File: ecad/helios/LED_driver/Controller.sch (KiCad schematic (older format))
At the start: 12 parts, among them J3 Conn_02x03_Odd_Even, SW1 SW_Push, U7 ATTINY24-20SSU, Y1 Crystal

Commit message: Finishes the schematics
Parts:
- J4: renamed from J3; Part Number (none) -> M20-8760342
- SW1: footprint (none) -> Buttons_Switches_THT:SW_PUSH_6mm; Part Number (none) -> 1825910-6
- Y1: value Crystal -> 10 MHz; Part Number (none) -> ABLS-10.000MHZ-B2-T
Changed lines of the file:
@@
 P 7000 4650
 F 0 "Y1" H 7000 4800 50  0000 C CNN
-F 1 "Crystal" H 7000 4500 50  0000 C CNN
+F 1 "10 MHz" H 7000 4500 50  0000 C CNN
 F 2 "Crystals:Crystal_SMD_HC49-SD" H 7000 4650 50  0001 C CNN
 F 3 "" H 7000 4650 50  0001 C CNN
+F 4 "ABLS-10.000MHZ-B2-T" H 7000 4650 60  0001 C CNN "Part Number"
 	1    7000 4650
 	0    1    1    0
@@
 	7700 4950 7500 4950
 $Comp
-L GND #PWR026
+L GND #PWR027
 U 1 1 5AB48C0D
 P 7900 4650
-F 0 "#PWR026" H 7900 4400 50  0001 C CNN
+F 0 "#PWR027" H 7900 4400 50  0001 C CNN
 F 1 "GND" H 7900 4500 50  0000 C CNN
 F 2 "" H 7900 4650 50  0001 C CNN
@@
 Connection ~ 7000 4850
 $Comp
-L Conn_02x03_Odd_Even J3
+L Conn_02x03_Odd_Even J4
 U 1 1 5AB48E51
 P 7300 2400
-F 0 "J3" H 7350 2600 50  0000 C CNN
+F 0 "J4" H 7350 2600 50  0000 C CNN
 F 1 "Conn_02x03_Odd_Even" H 7350 2200 50  0000 C CNN
 F 2 "Pin_Headers:Pin_Header_Straight_2x03_Pitch2.54mm_SMD" H 7300 2400 50  0001 C CNN
 F 3 "" H 7300 2400 50  0001 C CNN
+F 4 "M20-8760342" H 7300 2400 60  0001 C CNN "Part Number"
 	1    7300 2400
 	1    0    0    -1
@@
 	6500 2500 7100 2500
 $Comp
-L +5V #PWR027
+L +5V #PWR028
 U 1 1 5AB48FA1
 P 8050 2000
-F 0 "#PWR027" H 8050 1850 50  0001 C CNN
+F 0 "#PWR028" H 8050 1850 50  0001 C CNN
 F 1 "+5V" H 8050 2140 50  0000 C CNN
 F 2 "" H 8050 2000 50  0001 C CNN
@@
 	8050 2300 7600 2300
 $Comp
-L GND #PWR028
+L GND #PWR029
 U 1 1 5AB48FDE
 P 8050 2900
-F 0 "#PWR028" H 8050 2650 50  0001 C CNN
+F 0 "#PWR029" H 8050 2650 50  0001 C CNN
 F 1 "GND" H 8050 2750 50  0000 C CNN
 F 2 "" H 8050 2900 50  0001 C CNN
@@
 	2300 4900 2600 4900
 $Comp
-L +36V #PWR029
+L +36V #PWR030
 U 1 1 5AB49787
 P 6000 2350
-F 0 "#PWR029" H 6000 2200 50  0001 C CNN
+F 0 "#PWR030" H 6000 2200 50  0001 C CNN
 F 1 "+36V" H 6000 2490 50  0000 C CNN
 F 2 "" H 6000 2350 50  0001 C CNN
@@
 $EndComp
 $Comp
-L GND #PWR030
+L GND #PWR031
 U 1 1 5AB49BA2
 P 6000 3450
-F 0 "#PWR030" H 6000 3200 50  0001 C CNN
+F 0 "#PWR031" H 6000 3200 50  0001 C CNN
 F 1 "GND" H 6000 3300 50  0000 C CNN
 F 2 "" H 6000 3450 50  0001 C CNN
@@
 Connection ~ 2300 3700
 $Comp
-L +5V #PWR031
+L +5V #PWR032
 U 1 1 5AB49D08
 P 2300 2800
-F 0 "#PWR031" H 2300 2650 50  0001 C CNN
+F 0 "#PWR032" H 2300 2650 50  0001 C CNN
 F 1 "+5V" H 2300 2940 50  0000 C CNN
 F 2 "" H 2300 2800 50  0001 C CNN
@@
 F 0 "SW1" H 4500 5950 50  0000 L CNN
 F 1 "SW_Push" H 4450 5790 50  0000 C CNN
-F 2 "" H 4450 6050 50  0001 C CNN
+F 2 "Buttons_Switches_THT:SW_PUSH_6mm" H 4450 6050 50  0001 C CNN
 F 3 "" H 4450 6050 50  0001 C CNN
+F 4 "1825910-6" H 4450 5850 60  0001 C CNN "Part Number"
 	1    4450 5850
 	1    0    0    -1
@@
 	5200 5200 5200 5400
 $Comp
-L +5V #PWR032
+L +5V #PWR033
 U 1 1 5AB4A50E
 P 5050 5150
-F 0 "#PWR032" H 5050 5000 50  0001 C CNN
+F 0 "#PWR033" H 5050 5000 50  0001 C CNN
 F 1 "+5V" H 5050 5290 50  0000 C CNN
 F 2 "" H 5050 5150 50  0001 C CNN
@@
 Connection ~ 4900 5850
 $Comp
-L GND #PWR033
+L GND #PWR034
 U 1 1 5AB4A605
 P 4000 6050
-F 0 "#PWR033" H 4000 5800 50  0001 C CNN
+F 0 "#PWR034" H 4000 5800 50  0001 C CNN
 F 1 "GND" H 4000 5900 50  0000 C CNN
 F 2 "" H 4000 6050 50  0001 C CNN

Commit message: layouted the board
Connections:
- net EN36V: now also U7.11 ((PCINT2/AIN1/ADC2)PA2); no longer U7.12 ((PCINT1/AIN0/ADC1)PA1)
- net FLASH_IN: now also U7.13 ((PCINT0/AREF/ADC0)PA0); no longer U7.10 ((PCINT3/T0/ADC3)PA3)
- net GND: now also C36.2, U7.14 (GND)
- net IR_ON: now also U7.10 ((PCINT3/T0/ADC3)PA3); no longer U7.11 ((PCINT2/AIN1/ADC2)PA2)
- net V36_MEASURE: now reaches D8.2 (A), R36.2, R37.1
- net V36_MEASURE: now also U7.12 ((PCINT1/AIN0/ADC1)PA1); no longer U7.13 ((PCINT0/AREF/ADC0)PA0)
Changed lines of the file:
@@
 	4700 4100 5100 4100
 Wire Wire Line
-	4700 4200 5100 4200
+	4700 4200 5650 4200
 Wire Wire Line
 	4700 4900 6100 4900
@@
 Wire Wire Line
 	2300 3700 2600 3700
-Wire Wire Line
-	2300 4400 2300 4900
-Wire Wire Line
-	2300 4900 2600 4900
 $Comp
 L +36V #PWR030
@@
 Wire Wire Line
 	6000 2900 5750 2900
-Wire Wire Line
-	5750 2900 5750 3700
-Wire Wire Line
-	5750 3700 4700 3700
 Connection ~ 6000 2900
 Wire Wire Line
-	4400 3150 4950 3150
-Wire Wire Line
-	4950 3150 4950 3700
-Connection ~ 4950 3700
+	4400 3150 5750 3150
 Wire Wire Line
 	4100 3150 2300 3150
@@
 Text HLabel 5650 4300 2    60   Input ~ 0
 DATA_IN
-Text HLabel 5650 4000 2    60   Input ~ 0
+Text HLabel 5050 3700 2    60   Input ~ 0
 FLASH_IN
 Text HLabel 5650 4800 2    60   Output ~ 0
@@
 	4700 4800 5650 4800
 Wire Wire Line
-	4700 4000 5650 4000
-Wire Wire Line
 	4700 4300 5650 4300
-Text HLabel 5650 3900 2    60   Output ~ 0
+Text HLabel 5050 4000 2    60   Output ~ 0
 IR_ON
-Wire Wire Line
-	4700 3900 5650 3900
 NoConn ~ 4700 4400
-Text HLabel 5650 3800 2    60   Output ~ 0
+Text HLabel 5050 3900 2    60   Output ~ 0
 EN36V
-Wire Wire Line
-	4700 3800 5650 3800
+Connection ~ 5750 3150
+Text Label 4800 3150 0    60   ~ 0
+V36_MEASURE
+Wire Wire Line
+	4700 4000 5050 4000
+Wire Wire Line
+	4700 3800 5750 3800
+$Comp
+L GND #PWR035
+U 1 1 5AB6BFF7
+P 2300 5050
+F 0 "#PWR035" H 2300 4800 50  0001 C CNN
+F 1 "GND" H 2300 4900 50  0000 C CNN
+F 2 "" H 2300 5050 50  0001 C CNN
+F 3 "" H 2300 5050 50  0001 C CNN
+	1    2300 5050
+	1    0    0    -1
+$EndComp
+Wire Wire Line
+	2300 4400 2300 5050
+Wire Wire Line
+	2600 4900 2300 4900
+Connection ~ 2300 4900
+Wire Wire Line
+	4700 3700 5050 3700
+Wire Wire Line
+	5750 3800 5750 2900
+Wire Wire Line
+	4700 3900 5050 3900
 $EndSCHEMATC

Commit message: Improves the layout
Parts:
- added R12: 100, Resistors_SMD:R_0603, symbol R
- Y1: footprint Crystals:Crystal_SMD_HC49-SD -> Crystals:Crystal_SMD_TXC_7M-4pin_3.2x2.5mm; Part Number ABLS-10.000MHZ-B2-T -> 7V-10.000MAHJ-T
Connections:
- net DATA_IN: now also R12.1; no longer J4.4 (Pin_4), U7.7 ((PCINT6/SDA/DI/MOSI/OC1A/ADC6)PA6)
- net EN36V: now also U7.10 ((PCINT3/T0/ADC3)PA3); no longer U7.11 ((PCINT2/AIN1/ADC2)PA2)
- net FLASH_IN: now also U7.6 ((PCINT7/ICP/OC0B/ADC7)PA7); no longer U7.13 ((PCINT0/AREF/ADC0)PA0)
- net IR_ON: now also U7.11 ((PCINT2/AIN1/ADC2)PA2); no longer U7.10 ((PCINT3/T0/ADC3)PA3)
- new net ICSP_MOSI: J4.4 (Pin_4), R12.2, U7.7 ((PCINT6/SDA/DI/MOSI/OC1A/ADC6)PA6)
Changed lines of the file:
@@
 F 0 "Y1" H 7000 4800 50  0000 C CNN
 F 1 "10 MHz" H 7000 4500 50  0000 C CNN
-F 2 "Crystals:Crystal_SMD_HC49-SD" H 7000 4650 50  0001 C CNN
+F 2 "Crystals:Crystal_SMD_TXC_7M-4pin_3.2x2.5mm" H 7000 4650 50  0001 C CNN
 F 3 "" H 7000 4650 50  0001 C CNN
-F 4 "ABLS-10.000MHZ-B2-T" H 7000 4650 60  0001 C CNN "Part Number"
+F 4 "7V-10.000MAHJ-T" H 7000 4650 60  0001 C CNN "Part Number"
 	1    7000 4650
 	0    1    1    0
@@
 	7700 4950 7500 4950
 $Comp
-L GND #PWR027
+L GND #PWR031
 U 1 1 5AB48C0D
 P 7900 4650
-F 0 "#PWR027" H 7900 4400 50  0001 C CNN
+F 0 "#PWR031" H 7900 4400 50  0001 C CNN
 F 1 "GND" H 7900 4500 50  0000 C CNN
 F 2 "" H 7900 4650 50  0001 C CNN
@@
 	6500 2500 7100 2500
 $Comp
-L +5V #PWR028
+L +5V #PWR032
 U 1 1 5AB48FA1
 P 8050 2000
-F 0 "#PWR028" H 8050 1850 50  0001 C CNN
+F 0 "#PWR032" H 8050 1850 50  0001 C CNN
 F 1 "+5V" H 8050 2140 50  0000 C CNN
 F 2 "" H 8050 2000 50  0001 C CNN
@@
 	8050 2300 7600 2300
 $Comp
-L GND #PWR029
+L GND #PWR033
 U 1 1 5AB48FDE
 P 8050 2900
-F 0 "#PWR029" H 8050 2650 50  0001 C CNN
+F 0 "#PWR033" H 8050 2650 50  0001 C CNN
 F 1 "GND" H 8050 2750 50  0000 C CNN
 F 2 "" H 8050 2900 50  0001 C CNN
@@
 	2300 3700 2600 3700
 $Comp
-L +36V #PWR030
+L +36V #PWR034
 U 1 1 5AB49787
 P 6000 2350
-F 0 "#PWR030" H 6000 2200 50  0001 C CNN
+F 0 "#PWR034" H 6000 2200 50  0001 C CNN
 F 1 "+36V" H 6000 2490 50  0000 C CNN
 F 2 "" H 6000 2350 50  0001 C CNN
@@
 $EndComp
 $Comp
-L GND #PWR031
+L GND #PWR035
 U 1 1 5AB49BA2
 P 6000 3450
-F 0 "#PWR031" H 6000 3200 50  0001 C CNN
+F 0 "#PWR035" H 6000 3200 50  0001 C CNN
 F 1 "GND" H 6000 3300 50  0000 C CNN
 F 2 "" H 6000 3450 50  0001 C CNN
@@
 Connection ~ 2300 3700
 $Comp
-L +5V #PWR032
+L +5V #PWR036
 U 1 1 5AB49D08
 P 2300 2800
-F 0 "#PWR032" H 2300 2650 50  0001 C CNN
+F 0 "#PWR036" H 2300 2650 50  0001 C CNN
 F 1 "+5V" H 2300 2940 50  0000 C CNN
 F 2 "" H 2300 2800 50  0001 C CNN
@@
 	5200 5200 5200 5400
 $Comp
-L +5V #PWR033
+L +5V #PWR037
 U 1 1 5AB4A50E
 P 5050 5150
-F 0 "#PWR033" H 5050 5000 50  0001 C CNN
+F 0 "#PWR037" H 5050 5000 50  0001 C CNN
 F 1 "+5V" H 5050 5290 50  0000 C CNN
 F 2 "" H 5050 5150 50  0001 C CNN
@@
 Connection ~ 4900 5850
 $Comp
-L GND #PWR034
+L GND #PWR038
 U 1 1 5AB4A605
 P 4000 6050
-F 0 "#PWR034" H 4000 5800 50  0001 C CNN
+F 0 "#PWR038" H 4000 5800 50  0001 C CNN
 F 1 "GND" H 4000 5900 50  0000 C CNN
 F 2 "" H 4000 6050 50  0001 C CNN
@@
 Wire Wire Line
 	4000 5850 4250 5850
-Text HLabel 5650 4300 2    60   Input ~ 0
+Text HLabel 6450 4300 2    60   Input ~ 0
 DATA_IN
-Text HLabel 5050 3700 2    60   Input ~ 0
+Text HLabel 5050 4400 2    60   Input ~ 0
 FLASH_IN
 Text HLabel 5650 4800 2    60   Output ~ 0
@@
 	4700 4800 5650 4800
 Wire Wire Line
-	4700 4300 5650 4300
+	4700 4300 5750 4300
+Text HLabel 5050 3900 2    60   Output ~ 0
+IR_ON
+NoConn ~ 4700 3700
 Text HLabel 5050 4000 2    60   Output ~ 0
-IR_ON
-NoConn ~ 4700 4400
-Text HLabel 5050 3900 2    60   Output ~ 0
 EN36V
 Connection ~ 5750 3150
@@
 	4700 3800 5750 3800
 $Comp
-L GND #PWR035
+L GND #PWR039
 U 1 1 5AB6BFF7
 P 2300 5050
-F 0 "#PWR035" H 2300 4800 50  0001 C CNN
+F 0 "#PWR039" H 2300 4800 50  0001 C CNN
 F 1 "GND" H 2300 4900 50  0000 C CNN
 F 2 "" H 2300 5050 50  0001 C CNN
@@
 Connection ~ 2300 4900
 Wire Wire Line
-	4700 3700 5050 3700
-Wire Wire Line
 	5750 3800 5750 2900
 Wire Wire Line
 	4700 3900 5050 3900
+Wire Wire Line
+	4700 4400 5050 4400
+$Comp
+L R R12
+U 1 1 5ABBB03C
+P 5900 4300
+F 0 "R12" V 5980 4300 50  0000 C CNN
+F 1 "100" V 5900 4300 50  0000 C CNN
+F 2 "Resistors_SMD:R_0603" V 5830 4300 50  0001 C CNN
+F 3 "" H 5900 4300 50  0001 C CNN
+F 4 "RMCF0603FT100" H 5900 4300 60  0001 C CNN "Part Number"
+	1    5900 4300
+	0    1    1    0
+$EndComp
+Wire Wire Line
+	6050 4300 6450 4300
 $EndSCHEMATC

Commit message: Adds a nice master board
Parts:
- removed Y1: 10 MHz, Crystals:Crystal_SMD_TXC_7M-4pin_3.2x2.5mm, symbol Crystal
- added Y1: 10MHz, Crystals:Crystal_SMD_TXC_7M-4pin_3.2x2.5mm, symbol Crystal_GND24
- R36: value 100k -> 100K
- R38: value 10k -> 10K
- U7: Part Number (none) -> ATTINY24-20SSU
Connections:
- net GND: now also Y1.2, Y1.4
- net UV_ON: now reaches U7.13 ((PCINT0/AREF/ADC0)PA0)
- net at C37.2, U7.2 ((PCINT8/CLKI/XTAL1)PB0): now also Y1.1
- net at C38.2, U7.3 ((PCINT9/XTAL2)PB1): now also Y1.3
- no-connect marks 1 -> 0
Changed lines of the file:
@@
 F 2 "Housings_SOIC:SOIC-14_3.9x8.7mm_Pitch1.27mm" H 3650 4100 50  0001 C CIN
 F 3 "" H 3650 4300 50  0001 C CNN
+F 4 "ATTINY24-20SSU" H 3650 4300 60  0001 C CNN "Part Number"
 	1    3650 4300
 	1    0    0    -1
@@
 U 1 1 5AB4899B
 P 7350 4350
-F 0 "C37" H 7375 4450 50  0000 L CNN
-F 1 "18pF" H 7375 4250 50  0000 L CNN
+F 0 "C37" V 7250 4450 50  0000 L CNN
+F 1 "18pF" V 7150 4450 50  0000 L CNN
 F 2 "Capacitors_SMD:C_0603" H 7388 4200 50  0001 C CNN
 F 3 "" H 7350 4350 50  0001 C CNN
@@
 $EndComp
 $Comp
-L Crystal Y1
-U 1 1 5AB48A55
-P 7000 4650
-F 0 "Y1" H 7000 4800 50  0000 C CNN
-F 1 "10 MHz" H 7000 4500 50  0000 C CNN
-F 2 "Crystals:Crystal_SMD_TXC_7M-4pin_3.2x2.5mm" H 7000 4650 50  0001 C CNN
-F 3 "" H 7000 4650 50  0001 C CNN
-F 4 "7V-10.000MAHJ-T" H 7000 4650 60  0001 C CNN "Part Number"
-	1    7000 4650
-	0    1    1    0
-$EndComp
-$Comp
 L C C38
 U 1 1 5AB48B9E
 P 7350 4950
-F 0 "C38" H 7375 5050 50  0000 L CNN
-F 1 "18pF" H 7375 4850 50  0000 L CNN
+F 0 "C38" V 7550 5050 50  0000 L CNN
+F 1 "18pF" V 7450 5050 50  0000 L CNN
 F 2 "Capacitors_SMD:C_0603" H 7388 4800 50  0001 C CNN
 F 3 "" H 7350 4950 50  0001 C CNN
@@
 	7700 4950 7500 4950
 $Comp
-L GND #PWR031
+L GND #PWR036
 U 1 1 5AB48C0D
 P 7900 4650
-F 0 "#PWR031" H 7900 4400 50  0001 C CNN
+F 0 "#PWR036" H 7900 4400 50  0001 C CNN
 F 1 "GND" H 7900 4500 50  0000 C CNN
 F 2 "" H 7900 4650 50  0001 C CNN
@@
 $EndComp
 Wire Wire Line
-	7900 4650 7700 4650
+	7200 4650 7900 4650
 Connection ~ 7700 4650
 Wire Wire Line
@@
 	6500 2500 7100 2500
 $Comp
-L +5V #PWR032
+L +5V #PWR037
 U 1 1 5AB48FA1
 P 8050 2000
-F 0 "#PWR032" H 8050 1850 50  0001 C CNN
+F 0 "#PWR037" H 8050 1850 50  0001 C CNN
 F 1 "+5V" H 8050 2140 50  0000 C CNN
 F 2 "" H 8050 2000 50  0001 C CNN
@@
 	8050 2300 7600 2300
 $Comp
-L GND #PWR033
+L GND #PWR038
 U 1 1 5AB48FDE
 P 8050 2900
-F 0 "#PWR033" H 8050 2650 50  0001 C CNN
+F 0 "#PWR038" H 8050 2650 50  0001 C CNN
 F 1 "GND" H 8050 2750 50  0000 C CNN
 F 2 "" H 8050 2900 50  0001 C CNN
@@
 	2300 3700 2600 3700
 $Comp
-L +36V #PWR034
+L +36V #PWR039
 U 1 1 5AB49787
 P 6000 2350
-F 0 "#PWR034" H 6000 2200 50  0001 C CNN
+F 0 "#PWR039" H 6000 2200 50  0001 C CNN
 F 1 "+36V" H 6000 2490 50  0000 C CNN
 F 2 "" H 6000 2350 50  0001 C CNN
@@
 P 6000 2650
 F 0 "R36" V 6080 2650 50  0000 C CNN
-F 1 "100k" V 6000 2650 50  0000 C CNN
+F 1 "100K" V 6000 2650 50  0000 C CNN
 F 2 "Resistors_SMD:R_0603" V 5930 2650 50  0001 C CNN
 F 3 "" H 6000 2650 50  0001 C CNN
@@
 $EndComp
 $Comp
-L GND #PWR035
+L GND #PWR040
 U 1 1 5AB49BA2
 P 6000 3450
-F 0 "#PWR035" H 6000 3200 50  0001 C CNN
+F 0 "#PWR040" H 6000 3200 50  0001 C CNN
 F 1 "GND" H 6000 3300 50  0000 C CNN
 F 2 "" H 6000 3450 50  0001 C CNN
@@
 Connection ~ 2300 3700
 $Comp
-L +5V #PWR036
+L +5V #PWR041
 U 1 1 5AB49D08
 P 2300 2800
-F 0 "#PWR036" H 2300 2650 50  0001 C CNN
+F 0 "#PWR041" H 2300 2650 50  0001 C CNN
 F 1 "+5V" H 2300 2940 50  0000 C CNN
 F 2 "" H 2300 2800 50  0001 C CNN
@@
 P 4900 5550
 F 0 "R38" V 4980 5550 50  0000 C CNN
-F 1 "10k" V 4900 5550 50  0000 C CNN
+F 1 "10K" V 4900 5550 50  0000 C CNN
 F 2 "Resistors_SMD:R_0603" V 4830 5550 50  0001 C CNN
 F 3 "" H 4900 5550 50  0001 C CNN
@@
 	5200 5200 5200 5400
 $Comp
-L +5V #PWR037
+L +5V #PWR042
 U 1 1 5AB4A50E
 P 5050 5150
-F 0 "#PWR037" H 5050 5000 50  0001 C CNN
+F 0 "#PWR042" H 5050 5000 50  0001 C CNN
 F 1 "+5V" H 5050 5290 50  0000 C CNN
 F 2 "" H 5050 5150 50  0001 C CNN
@@
 Connection ~ 4900 5850
 $Comp
-L GND #PWR038
+L GND #PWR043
 U 1 1 5AB4A605
 P 4000 6050
-F 0 "#PWR038" H 4000 5800 50  0001 C CNN
+F 0 "#PWR043" H 4000 5800 50  0001 C CNN
 F 1 "GND" H 4000 5900 50  0000 C CNN
 F 2 "" H 4000 6050 50  0001 C CNN
@@
 Text HLabel 5050 3900 2    60   Output ~ 0
 IR_ON
-NoConn ~ 4700 3700
 Text HLabel 5050 4000 2    60   Output ~ 0
 EN36V
@@
 	4700 3800 5750 3800
 $Comp
-L GND #PWR039
+L GND #PWR044
 U 1 1 5AB6BFF7
 P 2300 5050
-F 0 "#PWR039" H 2300 4800 50  0001 C CNN
+F 0 "#PWR044" H 2300 4800 50  0001 C CNN
 F 1 "GND" H 2300 4900 50  0000 C CNN
 F 2 "" H 2300 5050 50  0001 C CNN
@@
 Wire Wire Line
 	6050 4300 6450 4300
+Text HLabel 5050 3700 2    60   Output ~ 0
+UV_ON
+Wire Wire Line
+	4700 3700 5050 3700
+$Comp
+L Crystal_GND24 Y1
+U 1 1 5AC532E0
+P 7000 4650
+F 0 "Y1" V 7250 4750 50  0000 L CNN
+F 1 "10MHz" V 7150 4750 50  0000 L CNN
+F 2 "Crystals:Crystal_SMD_TXC_7M-4pin_3.2x2.5mm" H 7000 4650 50  0001 C CNN
+F 3 "" H 7000 4650 50  0001 C CNN
+F 4 "7V-10.000MAHJ-T" H 7000 4650 60  0001 C CNN "Part Number"
+	1    7000 4650
+	0    1    1    0
+$EndComp
+$Comp
+L GND #PWR?
+U 1 1 5AC5364C
+P 6750 4650
+F 0 "#PWR?" H 6750 4400 50  0001 C CNN
+F 1 "GND" H 6750 4500 50  0000 C CNN
+F 2 "" H 6750 4650 50  0001 C CNN
+F 3 "" H 6750 4650 50  0001 C CNN
+	1    6750 4650
+	0    1    1    0
+$EndComp
+Wire Wire Line
+	6750 4650 6800 4650
 $EndSCHEMATC

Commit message: wip
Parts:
- J4: value Conn_02x03_Odd_Even -> M20-8760342
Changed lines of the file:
@@
 P 7300 2400
 F 0 "J4" H 7350 2600 50  0000 C CNN
-F 1 "Conn_02x03_Odd_Even" H 7350 2200 50  0000 C CNN
+F 1 "M20-8760342" H 7350 2200 50  0000 C CNN
 F 2 "Pin_Headers:Pin_Header_Straight_2x03_Pitch2.54mm_SMD" H 7300 2400 50  0001 C CNN
 F 3 "" H 7300 2400 50  0001 C CNN

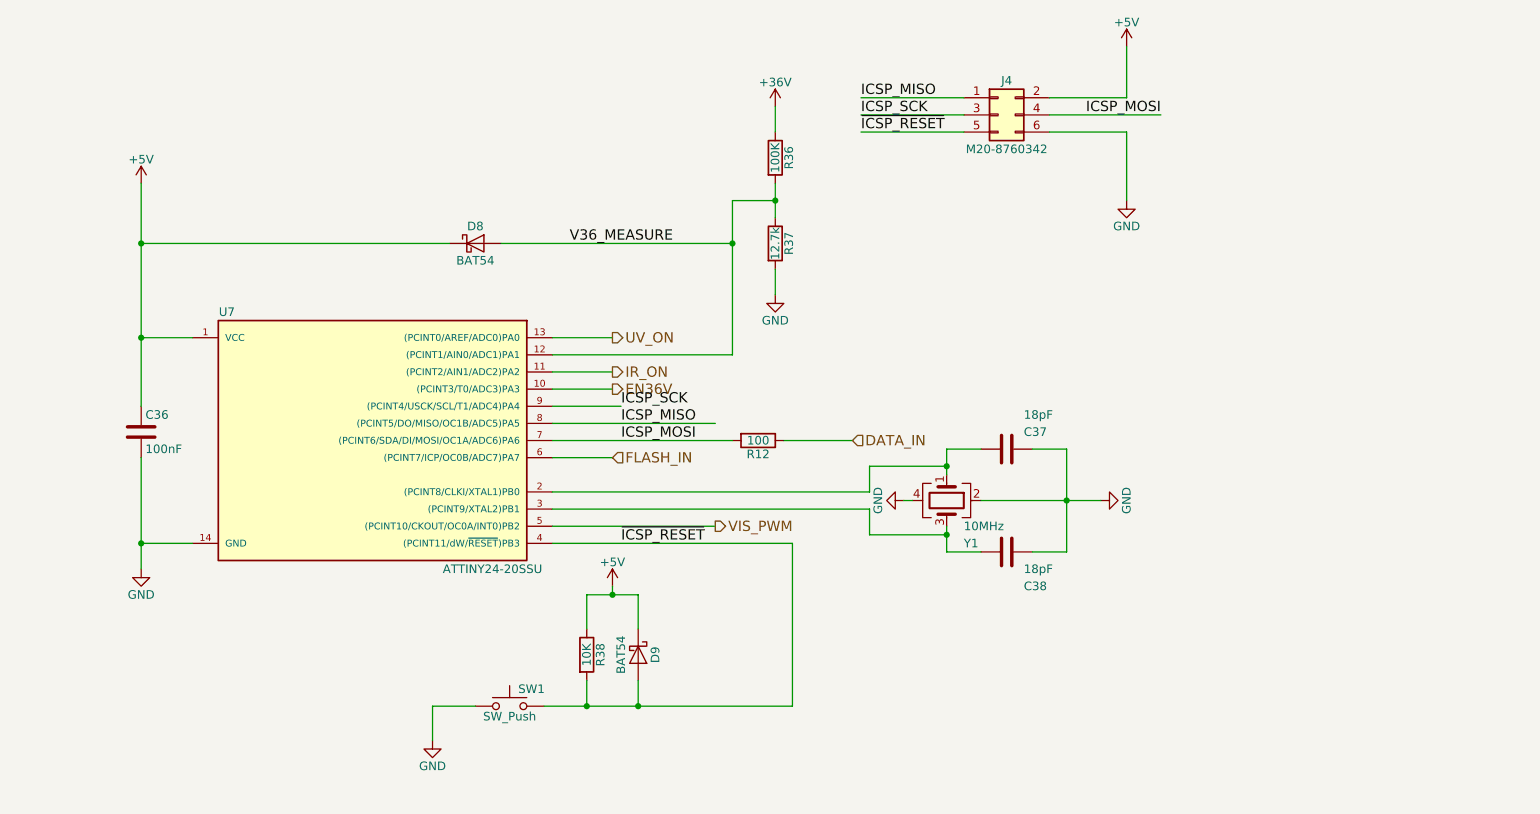
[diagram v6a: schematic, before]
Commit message: Replaces Attiny24 by atmeg328PB
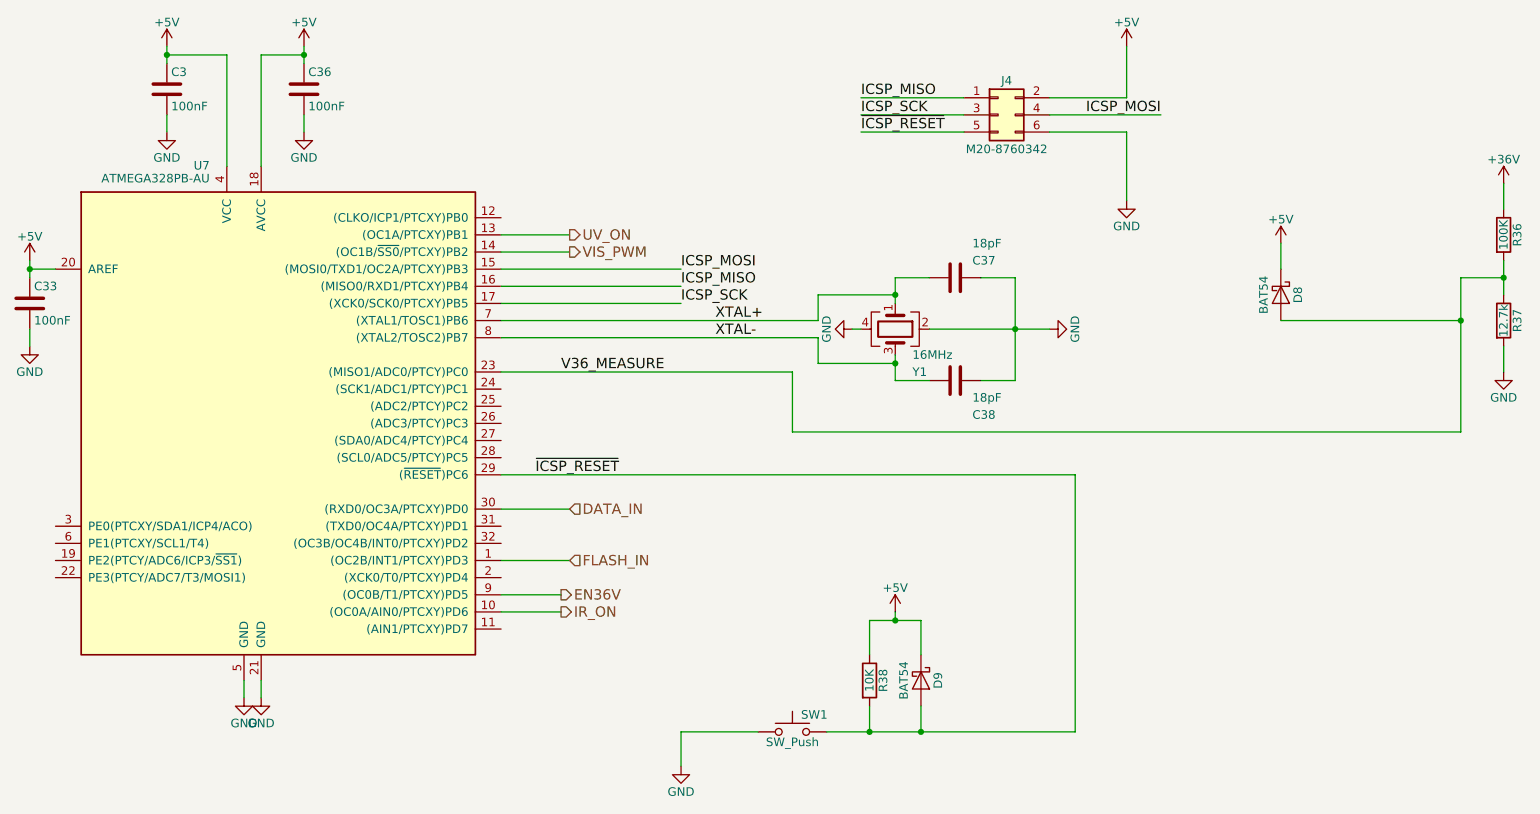
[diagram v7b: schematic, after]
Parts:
- removed R12: 100, Resistors_SMD:R_0603, symbol R
- removed U7: ATTINY24-20SSU, Housings_SOIC:SOIC-14_3.9x8.7mm_Pitch1.27mm, symbol ATTINY24-20SSU
- added C3, C33: 100nF, Capacitors_SMD:C_0603, symbol C
- added U7: ATMEGA328PB-AU, Housings_QFP:TQFP-32_7x7mm_Pitch0.8mm, symbol ATMEGA328PB-AU
- Y1: value 10MHz -> 16MHz; footprint Crystals:Crystal_SMD_TXC_7M-4pin_3.2x2.5mm -> Crystals:Crystal_SMD_SeikoEpson_FA238-4pin_3.2x2.5mm; Part Number 7V-10.000MAHJ-T -> FA-238 16.0000MB-C3
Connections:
- net +5V: now also C3.1, C33.1, U7.18 (AVCC), U7.20 (AREF), U7.4 (VCC)
- net DATA_IN: now also U7.30 ((RXD0/OC3A/PTCXY)PD0)
- net EN36V: now also U7.9 ((OC0B/T1/PTCXY)PD5)
- net FLASH_IN: now also U7.1 ((OC2B/INT1/PTCXY)PD3)
- net GND: now also C3.2, C33.2, U7.21 (GND), U7.5 (GND)
- net ICSP_MISO: now also U7.16 ((MISO0/RXD1/PTCXY)PB4)
- net ICSP_MOSI: now also U7.15 ((MOSI0/TXD1/OC2A/PTCXY)PB3)
- net ICSP_SCK: now also U7.17 ((XCK0/SCK0/PTCXY)PB5)
- net IR_ON: now also U7.10 ((OC0A/AIN0/PTCXY)PD6)
- net UV_ON: now also U7.13 ((OC1A/PTCXY)PB1)
- net V36_MEASURE: now also U7.23 ((MISO1/ADC0/PTCY)PC0)
- net VIS_PWM: now also U7.14 ((OC1B/~SS0~/PTCXY)PB2)
- net ~ICSP_RESET: now also U7.29 ((~RESET~)PC6)
- net XTAL+: now reaches C37.2, Y1.1
- net XTAL+: now also U7.7 ((XTAL1/TOSC1)PB6)
- net XTAL-: now reaches C38.2, Y1.3
- net XTAL-: now also U7.8 ((XTAL2/TOSC2)PB7)
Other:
- moved on the sheet: C36, C37, C38, D8, D9, R36, R37, R38, SW1, Y1
